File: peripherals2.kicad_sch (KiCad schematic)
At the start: 27 parts, among them J4 MSD-4-A, J5 DISPLAY CONN, Q2 T2N7002AK,LM, Q3 SL2301S, U8 GSDA213, U9 VEML3235SL

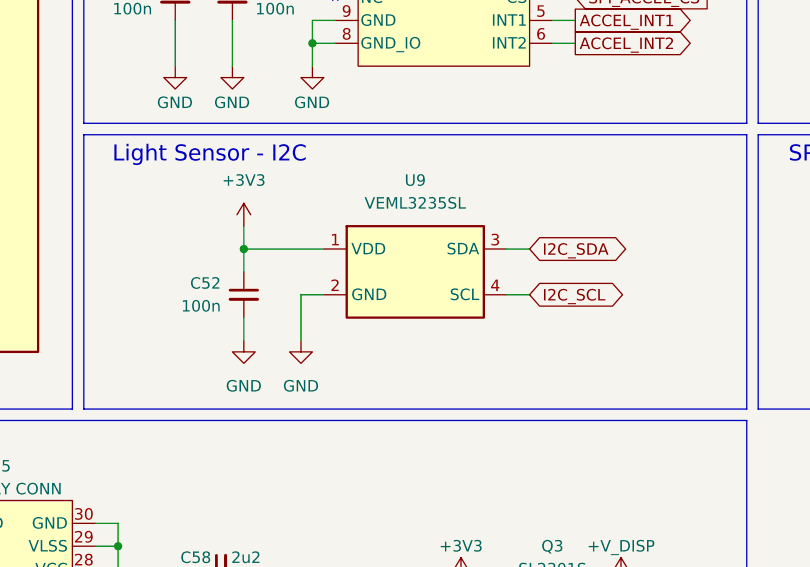
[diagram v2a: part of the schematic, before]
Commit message: feat: adds footprints and new light sensor
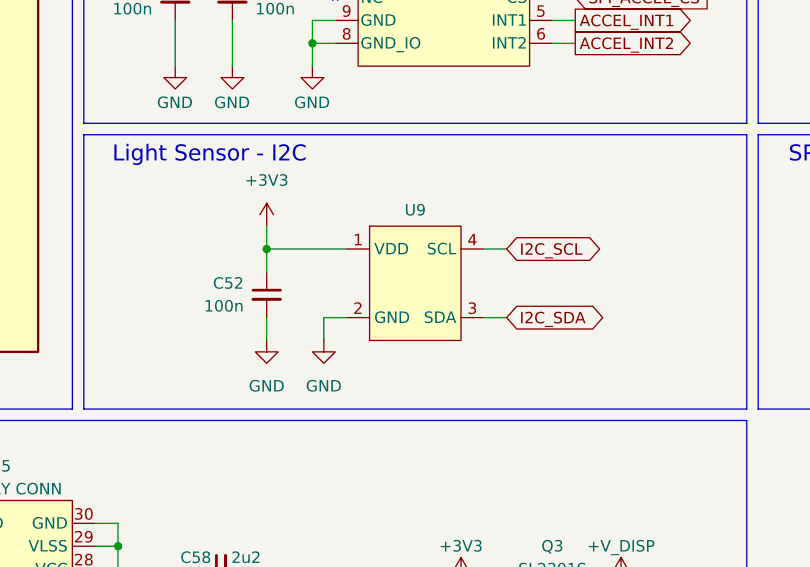
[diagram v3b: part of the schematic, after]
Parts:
- removed U9: VEML3235SL, symbol VEML3235SL:BL0937
- added U9: ~, peripherals2:LTR-329ALS-01_LTO-M, symbol peripherals2:LTR-329ALS-01
- J4: footprint CUI_MSD-4-A -> peripherals2:CUI_MSD-4-A
- U8: footprint (none) -> peripherals2:LGA12_GAS-M
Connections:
- net +3V3: now also U9.1 (VDD)
- net GND: now also U9.2 (GND)
- net I2C_SCL: now also U9.4 (SCL)
- net I2C_SDA: now also U9.3 (SDA)
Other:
- moved on the sheet: C52
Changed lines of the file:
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@@
 	)
 	(junction
-		(at 147.32 86.36)
+		(at 149.86 86.36)
 		(diameter 0)
 		(color 0 0 0 0)
@@
 	(wire
 		(pts
-			(xy 147.32 86.36) (xy 147.32 88.9)
+			(xy 149.86 86.36) (xy 149.86 88.9)
 		)
 		(stroke
@@
 	(wire
 		(pts
-			(xy 156.21 91.44) (xy 153.67 91.44)
+			(xy 158.75 93.98) (xy 156.21 93.98)
 		)
 		(stroke
@@
 	(wire
 		(pts
-			(xy 176.53 91.44) (xy 179.07 91.44)
+			(xy 173.99 86.36) (xy 176.53 86.36)
 		)
 		(stroke
@@
 	(wire
 		(pts
-			(xy 176.53 86.36) (xy 179.07 86.36)
+			(xy 173.99 93.98) (xy 176.53 93.98)
 		)
 		(stroke
@@
 	(wire
 		(pts
-			(xy 147.32 86.36) (xy 147.32 83.82)
+			(xy 149.86 86.36) (xy 149.86 83.82)
 		)
 		(stroke
@@
 	(wire
 		(pts
-			(xy 156.21 86.36) (xy 147.32 86.36)
+			(xy 158.75 86.36) (xy 149.86 86.36)
 		)
 		(stroke
@@
 	(wire
 		(pts
-			(xy 153.67 91.44) (xy 153.67 96.52)
+			(xy 156.21 93.98) (xy 156.21 96.52)
 		)
 		(stroke
@@
 	(wire
 		(pts
-			(xy 147.32 96.52) (xy 147.32 93.98)
+			(xy 149.86 96.52) (xy 149.86 93.98)
 		)
 		(stroke
@@
 	(global_label "I2C_SDA"
 		(shape bidirectional)
-		(at 179.07 86.36 0)
+		(at 176.53 93.98 0)
 		(fields_autoplaced yes)
 		(effects
@@
 		)
 		(property "Intersheetrefs" "${INTERSHEET_REFS}"
-			(at 188.5639 86.36 0)
+			(at 186.0239 93.98 0)
 			(effects
 				(font
@@
 	(global_label "I2C_SCL"
 		(shape bidirectional)
-		(at 179.07 91.44 0)
+		(at 176.53 86.36 0)
 		(fields_autoplaced yes)
 		(effects
@@
 		)
 		(property "Intersheetrefs" "${INTERSHEET_REFS}"
-			(at 188.5034 91.44 0)
+			(at 185.9634 86.36 0)
 			(effects
 				(font
@@
 			)
 		)
-		(property "Footprint" "CUI_MSD-4-A"
+		(property "Footprint" "peripherals2:CUI_MSD-4-A"
 			(at 114.3 69.85 0)
 			(effects
@@
 			)
 		)
-		(property "Datasheet" ""
+		(property "Datasheet" "https://www.digikey.com.br/en/products/detail/same-sky-formerly-cui-devices/MSD-4-A/21796808"
 			(at 114.3 69.85 0)
 			(effects
@@
 			)
 		)
-		(property "Footprint" ""
+		(property "Footprint" "peripherals2:LGA12_GAS-M"
 			(at 155.956 68.58 0)
 			(effects
@@
 	(symbol
 		(lib_id "power:GND")
-		(at 147.32 96.52 0)
+		(at 149.86 96.52 0)
 		(unit 1)
 		(exclude_from_sim no)
@@
 		(fields_autoplaced yes)
 		(property "Reference" "#PWR0133"
-			(at 147.32 102.87 0)
+			(at 149.86 102.87 0)
 			(effects
 				(font
@@
 		)
 		(property "Value" "GND"
-			(at 147.32 101.6 0)
+			(at 149.86 101.6 0)
 			(effects
 				(font
@@
 		)
 		(property "Footprint" ""
-			(at 147.32 96.52 0)
+			(at 149.86 96.52 0)
 			(effects
 				(font
@@
 		)
 		(property "Datasheet" ""
-			(at 147.32 96.52 0)
+			(at 149.86 96.52 0)
 			(effects
 				(font
@@
 		)
 		(property "Description" "Power symbol creates a global label with name \"GND\" , ground"
-			(at 147.32 96.52 0)
+			(at 149.86 96.52 0)
 			(effects
 				(font
@@
 	(symbol
 		(lib_id "Device:C_Small")
-		(at 147.32 91.44 0)
+		(at 149.86 91.44 0)
 		(unit 1)
 		(exclude_from_sim no)
@@
 		(fields_autoplaced yes)
 		(property "Reference" "C52"
-			(at 144.78 90.1762 0)
+			(at 147.32 90.1762 0)
 			(effects
 				(font
@@
 		)
 		(property "Value" "100n"
-			(at 144.78 92.7162 0)
+			(at 147.32 92.7162 0)
 			(effects
 				(font
@@
 		)
 		(property "Footprint" "Capacitor_SMD:C_0402_1005Metric"
-			(at 147.32 91.44 0)
+			(at 149.86 91.44 0)
 			(effects
 				(font
@@
 		)
 		(property "Datasheet" "https://www.digikey.com.br/en/products/detail/samsung-electro-mechanics/CL05B104KA5NNNC/5961204?s=N4IgTCBcDaIMIBkAMBWAQgRiQFgNIEEUA5EuEAXQF8g"
-			(at 147.32 91.44 0)
+			(at 149.86 91.44 0)
 			(effects
 				(font
@@
 		)
 		(property "Description" "Unpolarized capacitor, small symbol"
-			(at 147.32 91.44 0)
+			(at 149.86 91.44 0)
 			(effects
 				(font
@@
 		)
 		(property "MPN" "CL05B104KA5NNNC"
-			(at 147.32 91.44 0)
+			(at 149.86 91.44 0)
 			(effects
 				(font
@@
 	)
 	(symbol
-		(lib_id "VEML3235SL:BL0937")
-		(at 166.37 88.9 0)
-		(unit 1)
-		(exclude_from_sim no)
-		(in_bom yes)
-		(on_board yes)
-		(dnp no)
-		(fields_autoplaced yes)
-		(property "Reference" "U9"
-			(at 166.37 78.74 0)
-			(effects
-				(font
-					(size 1.27 1.27)
-				)
-			)
-		)
-		(property "Value" "VEML3235SL"
-			(at 166.37 81.28 0)
-			(effects
-				(font
-					(size 1.27 1.27)
-				)
-			)
-		)
-		(property "Footprint" ""
-			(at 168.91 106.68 0)
-			(effects
-				(font
-					(size 1.27 1.27)
-				)
-				(hide yes)
-			)
-		)
-		(property "Datasheet" ""
-			(at 180.594 102.108 0)
-			(effects
-				(font
-					(size 1.27 1.27)
-				)
-				(hide yes)
-			)
-		)
-		(property "Description" ""
-			(at 169.926 112.268 0)
-			(effects
-				(font
-					(size 1.27 1.27)
-				)
-				(hide yes)
-			)
-		)
-		(pin "2"
-		)
-		(pin "1"
-		)
-		(pin "4"
-		)
-		(pin "3"
-		)
-		(instances
-			(project ""
-				(path "/b90666d0-8852-4bb1-832d-f9d855027372/e26c05ee-f364-47de-be04-e77902e037c8"
-					(reference "U9")
-					(unit 1)
-				)
-			)
-		)
-	)
-	(symbol
 		(lib_id "Device:R_Small_US")
 		(at 214.63 55.88 0)
@@
 	(symbol
 		(lib_id "power:GND")
-		(at 153.67 96.52 0)
+		(at 156.21 96.52 0)
 		(unit 1)
 		(exclude_from_sim no)
@@
 		(fields_autoplaced yes)
 		(property "Reference" "#PWR0134"
-			(at 153.67 102.87 0)
+			(at 156.21 102.87 0)
 			(effects
 				(font
@@
 		)
 		(property "Value" "GND"
-			(at 153.67 101.6 0)
+			(at 156.21 101.6 0)
 			(effects
 				(font
@@
 		)
 		(property "Footprint" ""
-			(at 153.67 96.52 0)
+			(at 156.21 96.52 0)
 			(effects
 				(font
@@
 		)
 		(property "Datasheet" ""
-			(at 153.67 96.52 0)
+			(at 156.21 96.52 0)
 			(effects
 				(font
@@
 		)
 		(property "Description" "Power symbol creates a global label with name \"GND\" , ground"
-			(at 153.67 96.52 0)
+			(at 156.21 96.52 0)
 			(effects
 				(font
@@
 	)
 	(symbol
+		(lib_id "peripherals2:LTR-329ALS-01")
+		(at 166.37 90.17 0)
+		(unit 1)
+		(exclude_from_sim no)
+		(in_bom yes)
+		(on_board yes)
+		(dnp no)
+		(property "Reference" "U9"
+			(at 166.37 82.042 0)
+			(effects
+				(font
+					(size 1.27 1.27)
+				)
+			)
+		)
+		(property "Value" "~"
+			(at 166.37 82.55 0)
+			(effects
+				(font
+					(size 1.27 1.27)
+				)
+			)
+		)
+		(property "Footprint" "peripherals2:LTR-329ALS-01_LTO-M"
+			(at 166.37 90.17 0)
+			(effects
+				(font
+					(size 1.27 1.27)
+				)
+				(hide yes)
+			)
+		)
+		(property "Datasheet" "https://www.digikey.com.br/en/products/detail/lite-on-inc/ltr-329als-01/4847334"
+			(at 166.37 90.17 0)
+			(effects
+				(font
+					(size 1.27 1.27)
+				)
+				(hide yes)
+			)
+		)
+		(property "Description" ""
+			(at 166.37 90.17 0)
+			(effects
+				(font
+					(size 1.27 1.27)
+				)
+				(hide yes)
+			)
+		)
+		(property "MPN" "LTR-329ALS-01"
+			(at 166.37 90.17 0)
+			(effects
+				(font
+					(size 1.27 1.27)
+				)
+				(hide yes)
+			)
+		)
+		(pin "1"
+		)
+		(pin "4"
+		)
+		(pin "2"
+		)
+		(pin "3"
+		)
+		(instances
+			(project ""
+				(path "/b90666d0-8852-4bb1-832d-f9d855027372/e26c05ee-f364-47de-be04-e77902e037c8"
+					(reference "U9")
+					(unit 1)
+				)
+			)
+		)
+	)
+	(symbol
 		(lib_id "power:GND")
 		(at 181.61 148.59 0)
@@
 	(symbol
 		(lib_id "power:+3V3")
-		(at 147.32 83.82 0)
+		(at 149.86 83.82 0)
 		(unit 1)
 		(exclude_from_sim no)
@@
 		(fields_autoplaced yes)
 		(property "Reference" "#PWR0132"
-			(at 147.32 87.63 0)
+			(at 149.86 87.63 0)
 			(effects
 				(font
@@
 		)
 		(property "Value" "+3V3"
-			(at 147.32 78.74 0)
+			(at 149.86 78.74 0)
 			(effects
 				(font
@@
 		)
 		(property "Footprint" ""
-			(at 147.32 83.82 0)
+			(at 149.86 83.82 0)
 			(effects
 				(font
@@
 		)
 		(property "Datasheet" ""
-			(at 147.32 83.82 0)
+			(at 149.86 83.82 0)
 			(effects
 				(font
@@
 		)
 		(property "Description" "Power symbol creates a global label with name \"+3V3\""
-			(at 147.32 83.82 0)
+			(at 149.86 83.82 0)
 			(effects
 				(font

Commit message: feat: connects all global labels
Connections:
- net DISPLAY_RST renamed ~{DISPLAY_RST}
- net SPI_ACCEL_CS renamed ~{SPI_ACCEL_CS}
- net SPI_DISPLAY_CS renamed ~{SPI_DISPLAY_CS}
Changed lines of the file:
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@@
 		)
 	)
-	(global_label "SPI_DISPLAY_CS"
+	(global_label "~{SPI_DISPLAY_CS}"
 		(shape input)
 		(at 105.41 147.32 180)
@@
 		)
 	)
-	(global_label "SPI_ACCEL_CS"
+	(global_label "~{SPI_ACCEL_CS}"
 		(shape input)
 		(at 184.15 58.42 0)
@@
 		)
 	)
-	(global_label "DISPLAY_RST"
+	(global_label "~{DISPLAY_RST}"
 		(shape input)
 		(at 78.74 149.86 180)

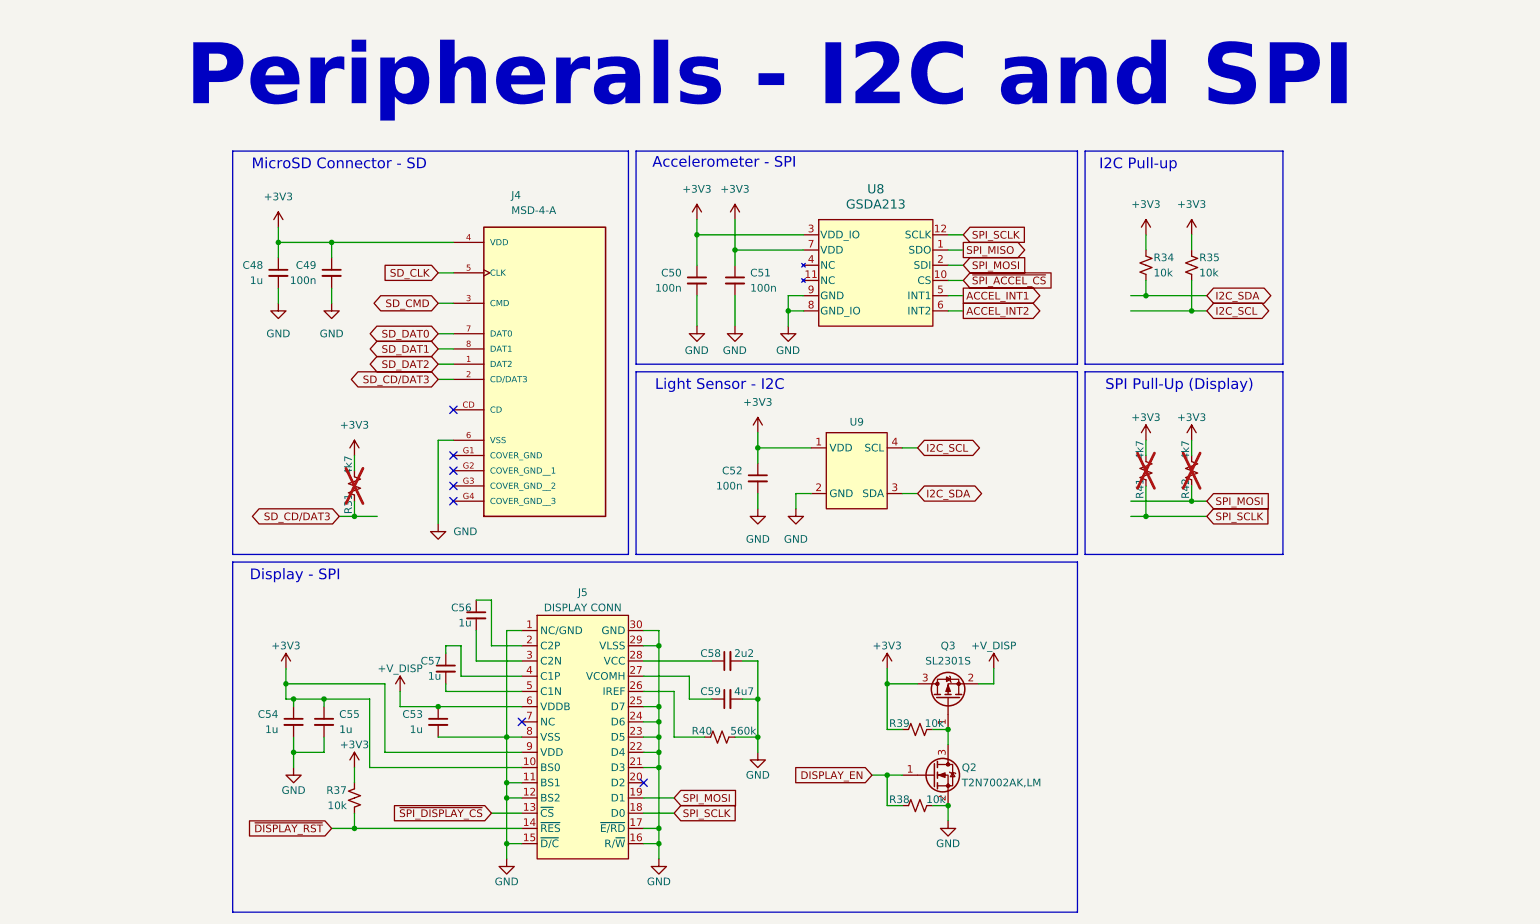
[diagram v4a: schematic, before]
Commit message: chore: makes changes for DRC check compliance
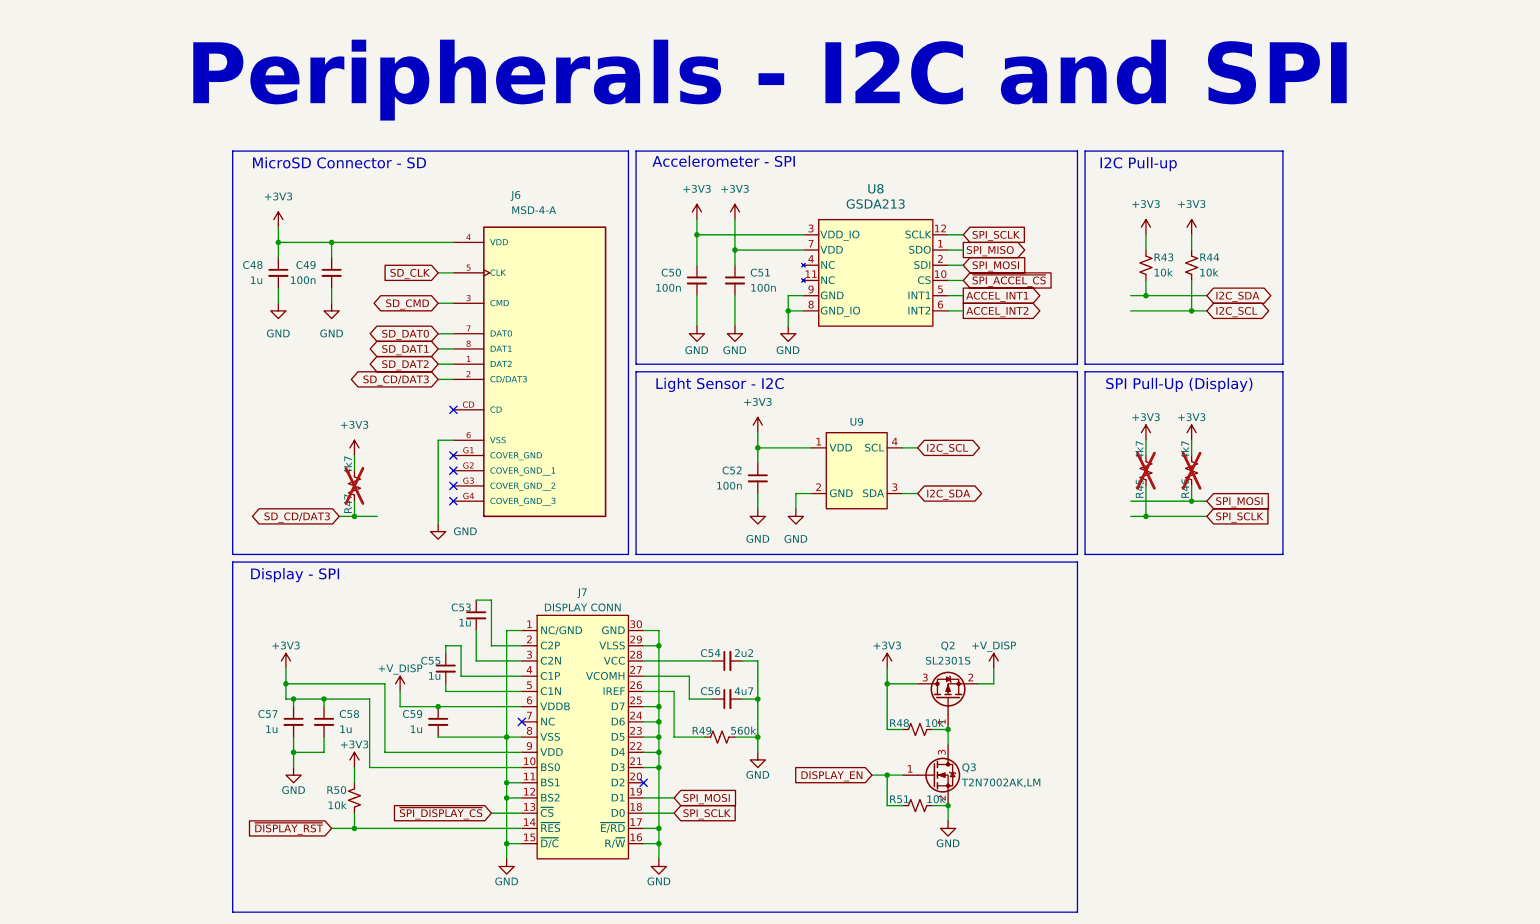
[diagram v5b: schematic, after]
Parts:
- renumbered C56 to C53, C58 to C54, C57 to C55, C59 to C56, C54 to C57, C55 to C58, C53 to C59, J4 to J6, J5 to J7, Q3 to Q2, Q2 to Q3, R34 to R43, R35 to R44, R41 to R45, R42 to R46, R31 to R47, R39 to R48, R40 to R49, R37 to R50, R38 to R51

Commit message: feat: adds testpoints
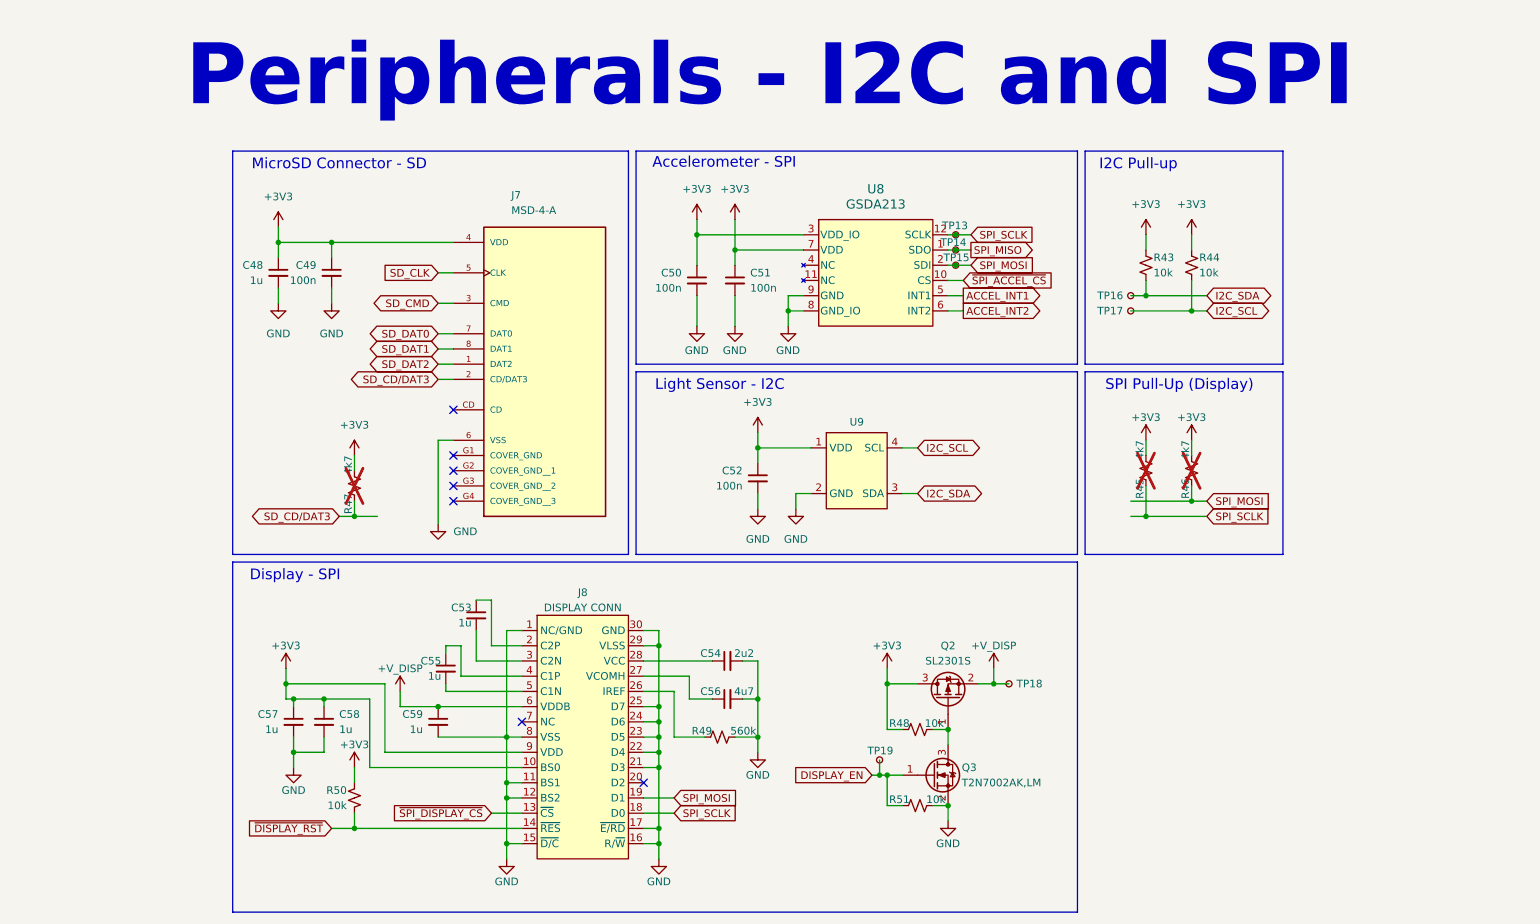
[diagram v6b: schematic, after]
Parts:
- added TP13, TP14, TP15, TP16, TP17, TP18, TP19: TestPoint_Small, TestPoint:TestPoint_Pad_D1.0mm, symbol Connector:TestPoint_Small
- J7: renamed from J6; MPN (none) -> MSD-4-A
- renumbered J7 to J8
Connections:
- net +V_DISP: now also TP18.1
- net DISPLAY_EN: now also TP19.1
- net I2C_SCL: now also TP17.1
- net I2C_SDA: now also TP16.1
- net SPI_MISO: now also TP14.1
- net SPI_MOSI: now also TP15.1
- net SPI_SCLK: now also TP13.1
